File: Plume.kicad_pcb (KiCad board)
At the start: 4 copper layers, 0 parts

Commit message: Added RGB LED, added motor connectors, added test points, imported all 3D models
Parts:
- added C1001: 10u X5R 16V, Capacitor_SMD:C_0603_1608Metric, F.Cu at (188.8, 130.8)
- added C1002: 100n X7R 16V, Capacitor_SMD:C_0402_1005Metric, F.Cu at (192.2, 130.5)
- added C1003: 100n X7R 16V, Capacitor_SMD:C_0402_1005Metric, F.Cu at (192.2, 132.4)
- added C1101: 10u X5R 16V, Capacitor_SMD:C_0603_1608Metric, F.Cu at (188.7, 105.7)
- added C1102: 100n X7R 16V, Capacitor_SMD:C_0402_1005Metric, F.Cu at (185.2, 108.0)
- added C1103: 100n X7R 16V, Capacitor_SMD:C_0402_1005Metric, F.Cu at (185.2, 106.1)
- added C1201: 10u X5R 16V, Capacitor_SMD:C_0603_1608Metric, F.Cu at (200.4, 105.7)
- added C1202: 100n X7R 16V, Capacitor_SMD:C_0402_1005Metric, F.Cu at (196.9, 108.0)
- added C1203: 100n X7R 16V, Capacitor_SMD:C_0402_1005Metric, F.Cu at (196.9, 106.1)
- added C1301: 10u X5R 16V, Capacitor_SMD:C_0603_1608Metric, F.Cu at (188.7, 93.3)
- added C1302: 100n X7R 16V, Capacitor_SMD:C_0402_1005Metric, F.Cu at (185.2, 95.7)
- added C1303: 100n X7R 16V, Capacitor_SMD:C_0402_1005Metric, F.Cu at (185.2, 93.7)
- added C1401: 10u X5R 16V, Capacitor_SMD:C_0603_1608Metric, F.Cu at (200.4, 93.3)
- added C1402: 100n X7R 16V, Capacitor_SMD:C_0402_1005Metric, F.Cu at (196.9, 95.7)
- added C1403: 100n X7R 16V, Capacitor_SMD:C_0402_1005Metric, F.Cu at (196.9, 93.7)
- added C1501: 10u X5R 16V, Capacitor_SMD:C_0603_1608Metric, F.Cu at (165.1, 93.3)
- added C1502: 100n X7R 16V, Capacitor_SMD:C_0402_1005Metric, F.Cu at (161.6, 95.7)
- added C1503: 100n X7R 16V, Capacitor_SMD:C_0402_1005Metric, F.Cu at (161.6, 93.7)
- added C1601: 10u X5R 16V, Capacitor_SMD:C_0603_1608Metric, F.Cu at (176.9, 93.3)
- added C1602: 100n X7R 16V, Capacitor_SMD:C_0402_1005Metric, F.Cu at (173.4, 95.7)
- added C1603: 100n X7R 16V, Capacitor_SMD:C_0402_1005Metric, F.Cu at (173.4, 93.7)
- added C1701: 10u X5R 16V, Capacitor_SMD:C_0603_1608Metric, F.Cu at (176.9, 105.7)
- added C1702: 100n X7R 16V, Capacitor_SMD:C_0402_1005Metric, F.Cu at (173.4, 108.0)
- added C1703: 100n X7R 16V, Capacitor_SMD:C_0402_1005Metric, F.Cu at (173.4, 106.1)
- added C1801: 10u X5R 16V, Capacitor_SMD:C_0603_1608Metric, F.Cu at (188.7, 118.0)
- added C1802: 100n X7R 16V, Capacitor_SMD:C_0402_1005Metric, F.Cu at (185.2, 120.3)
- added C1803: 100n X7R 16V, Capacitor_SMD:C_0402_1005Metric, F.Cu at (185.2, 118.4)
- added C1901: 10u X5R 16V, Capacitor_SMD:C_0603_1608Metric, F.Cu at (153.3, 130.3)
- added C1902: 100n X7R 16V, Capacitor_SMD:C_0402_1005Metric, F.Cu at (149.9, 132.7)
- added C1903: 100n X7R 16V, Capacitor_SMD:C_0402_1005Metric, F.Cu at (149.9, 130.7)
- added C2001: 10u X5R 16V, Capacitor_SMD:C_0603_1608Metric, F.Cu at (153.3, 118.0)
- added C2002: 100n X7R 16V, Capacitor_SMD:C_0402_1005Metric, F.Cu at (149.9, 120.3)
- added C2003: 100n X7R 16V, Capacitor_SMD:C_0402_1005Metric, F.Cu at (149.9, 118.4)
- added C2101: 10u X5R 16V, Capacitor_SMD:C_0603_1608Metric, F.Cu at (153.3, 93.3)
- added C2102: 100n X7R 16V, Capacitor_SMD:C_0402_1005Metric, F.Cu at (149.9, 95.7)
- added C2103: 100n X7R 16V, Capacitor_SMD:C_0402_1005Metric, F.Cu at (149.9, 93.7)
- added C2201: 10u X5R 16V, Capacitor_SMD:C_0603_1608Metric, F.Cu at (165.1, 130.3)
- added C2202: 100n X7R 16V, Capacitor_SMD:C_0402_1005Metric, F.Cu at (161.6, 132.7)
- added C2203: 100n X7R 16V, Capacitor_SMD:C_0402_1005Metric, F.Cu at (161.6, 130.7)
- added C2301: 10u X5R 16V, Capacitor_SMD:C_0603_1608Metric, F.Cu at (153.3, 105.7)
- added C2302: 100n X7R 16V, Capacitor_SMD:C_0402_1005Metric, F.Cu at (149.9, 108.0)
- added C2303: 100n X7R 16V, Capacitor_SMD:C_0402_1005Metric, F.Cu at (149.9, 106.1)
- added C2401: 10u X5R 16V, Capacitor_SMD:C_0603_1608Metric, F.Cu at (165.1, 105.7)
- added C2402: 100n X7R 16V, Capacitor_SMD:C_0402_1005Metric, F.Cu at (161.6, 108.0)
- added C2403: 100n X7R 16V, Capacitor_SMD:C_0402_1005Metric, F.Cu at (161.6, 106.1)
- added C2501: 10u X5R 16V, Capacitor_SMD:C_0603_1608Metric, F.Cu at (176.9, 118.0)
- added C2502: 100n X7R 16V, Capacitor_SMD:C_0402_1005Metric, F.Cu at (173.4, 120.3)
- added C2503: 100n X7R 16V, Capacitor_SMD:C_0402_1005Metric, F.Cu at (173.4, 118.4)
- added C2601: 10u X5R 16V, Capacitor_SMD:C_0603_1608Metric, F.Cu at (165.1, 118.0)
- added C2602: 100n X7R 16V, Capacitor_SMD:C_0402_1005Metric, F.Cu at (161.6, 120.3)
- added C2603: 100n X7R 16V, Capacitor_SMD:C_0402_1005Metric, F.Cu at (161.6, 118.4)
- added C2701: 10u X5R 16V, Capacitor_SMD:C_0603_1608Metric, F.Cu at (176.9, 130.3)
- added C2702: 100n X7R 16V, Capacitor_SMD:C_0402_1005Metric, F.Cu at (173.4, 132.7)
- added C2703: 100n X7R 16V, Capacitor_SMD:C_0402_1005Metric, F.Cu at (173.4, 130.7)
- added C2801: 220n X7R 16V, Capacitor_SMD:C_0603_1608Metric, F.Cu at (192.3, 74.9)
- added C2802: 2u2 X7R 16V, Capacitor_SMD:C_0603_1608Metric, F.Cu at (192.3, 72.4)
- added C2803: 100n X7R 16V, Capacitor_SMD:C_0402_1005Metric, F.Cu at (199.7, 75.1)
- added C2804: 2u2 X7R 16V, Capacitor_SMD:C_0603_1608Metric, F.Cu at (192.3, 69.9)
- added C2901: 1n X7R 1kV, Capacitor_SMD:C_0603_1608Metric, F.Cu at (161.9, 47.3)
- added C2902: 1n X7R 1kV, Capacitor_SMD:C_0603_1608Metric, F.Cu at (161.9, 49.9)
- added C2903: 1n X7R 1kV, Capacitor_SMD:C_0603_1608Metric, F.Cu at (161.9, 52.4)
- added C2904: 1n X7R 1kV, Capacitor_SMD:C_0603_1608Metric, F.Cu at (161.9, 54.9)
- added C401: 100n X7R 16V, Capacitor_SMD:C_0402_1005Metric, F.Cu at (197.8, 52.1)
- added C402: 100n X7R 16V, Capacitor_SMD:C_0402_1005Metric, F.Cu at (197.8, 54.1)
- added C403: 4u7 X7R 16V, Capacitor_SMD:C_0603_1608Metric, F.Cu at (201.2, 52.4)
- added C404: 100n X7R 16V, Capacitor_SMD:C_0402_1005Metric, F.Cu at (197.8, 56.1)
- added C501: 4u7 X7R 16V, Capacitor_SMD:C_0603_1608Metric, F.Cu at (216.6, 60.7)
- added C502: 100n X7R 16V, Capacitor_SMD:C_0402_1005Metric, F.Cu at (220.6, 53.8)
- added C503: 4u7 X7R 16V, Capacitor_SMD:C_0603_1608Metric, F.Cu at (216.6, 58.2)
- added C601: 100n X7R 16V, Capacitor_SMD:C_0402_1005Metric, F.Cu at (171.4, 47.1)
- added C602: 10u X5R 16V, Capacitor_SMD:C_0603_1608Metric, F.Cu at (167.9, 59.9)
- added C603: 1u X7R 16V, Capacitor_SMD:C_0603_1608Metric, F.Cu at (167.9, 57.4)
- added C604: 100n X7R 16V, Capacitor_SMD:C_0402_1005Metric, F.Cu at (171.4, 49.0)
- added C605: 100n X7R 16V, Capacitor_SMD:C_0402_1005Metric, F.Cu at (171.4, 51.0)
- added C606: 470n X7R 25V, Capacitor_SMD:C_0603_1608Metric, F.Cu at (167.9, 47.3)
- added C607: 22n X7R 25V, Capacitor_SMD:C_0402_1005Metric, F.Cu at (171.4, 55.0)
- added C608: 10n C0G 25V, Capacitor_SMD:C_0402_1005Metric, F.Cu at (171.4, 58.9)
- added C609: 470n X7R 25V, Capacitor_SMD:C_0603_1608Metric, F.Cu at (167.9, 54.9)
- added C610: 470n X7R 25V, Capacitor_SMD:C_0603_1608Metric, F.Cu at (167.9, 52.4)
- added C611: 470n X7R 25V, Capacitor_SMD:C_0603_1608Metric, F.Cu at (167.9, 49.9)
- added C612: 22n X7R 25V, Capacitor_SMD:C_0402_1005Metric, F.Cu at (171.4, 53.0)
- added C613: 10n C0G 25V, Capacitor_SMD:C_0402_1005Metric, F.Cu at (171.4, 56.9)
- added C701: 100n X7R 16V, Capacitor_SMD:C_0402_1005Metric, F.Cu at (167.4, 80.0)
- added C702: 1u X7R 16V, Capacitor_SMD:C_0603_1608Metric, F.Cu at (171.0, 77.7)
- added C703: 10u X5R 16V, Capacitor_SMD:C_0603_1608Metric, F.Cu at (171.0, 80.3)
- added C801: 1u X7R 16V, Capacitor_SMD:C_0603_1608Metric, F.Cu at (213.5, 73.4)
- added C802: 100n X7R 16V, Capacitor_SMD:C_0402_1005Metric, F.Cu at (213.0, 75.6)
- added D2801: IN-PI22TAT5R5G5B, 0_Plume:INPI22TAT5R5G5B, F.Cu at (197.4, 71.4)
- added D601: TVS SMF5.0A, 0_Plume:D_SOD-123FL, F.Cu at (181.1, 63.2)
- added D701: Schottky 1N5819W, Diode_SMD:Nexperia_CFP3_SOD-123W, F.Cu at (168.7, 70.2)
- added H2901: M2.5 (2.7mm), MountingHole:MountingHole_2.5mm_Pad_Via, F.Cu at (156.6, 69.0)
- added H2902: M2.5 (2.7mm), MountingHole:MountingHole_2.5mm_Pad_Via, F.Cu at (156.6, 49.4)
- added H2903: M2.5 (2.7mm), MountingHole:MountingHole_2.5mm_Pad_Via, F.Cu at (156.6, 55.9)
- added H2904: M2.5 (2.7mm), MountingHole:MountingHole_2.5mm_Pad_Via, F.Cu at (156.6, 62.5)
- added IC1001: DRV8214RTER, 0_Plume:WQFN-16-1EP_3x3mm_P0.5mm_EP1.68x1.68mm_ThermalVias, F.Cu at (189.4, 126.8)
- added IC1101: DRV8214RTER, 0_Plume:WQFN-16-1EP_3x3mm_P0.5mm_EP1.68x1.68mm_ThermalVias, F.Cu at (189.3, 101.8)
- added IC1201: DRV8214RTER, 0_Plume:WQFN-16-1EP_3x3mm_P0.5mm_EP1.68x1.68mm_ThermalVias, F.Cu at (201.1, 101.8)
- added IC1301: DRV8214RTER, 0_Plume:WQFN-16-1EP_3x3mm_P0.5mm_EP1.68x1.68mm_ThermalVias, F.Cu at (189.3, 89.4)
- added IC1401: DRV8214RTER, 0_Plume:WQFN-16-1EP_3x3mm_P0.5mm_EP1.68x1.68mm_ThermalVias, F.Cu at (201.1, 89.4)
- added IC1501: DRV8214RTER, 0_Plume:WQFN-16-1EP_3x3mm_P0.5mm_EP1.68x1.68mm_ThermalVias, F.Cu at (165.8, 89.4)
- added IC1601: DRV8214RTER, 0_Plume:WQFN-16-1EP_3x3mm_P0.5mm_EP1.68x1.68mm_ThermalVias, F.Cu at (177.5, 89.4)
- added IC1701: DRV8214RTER, 0_Plume:WQFN-16-1EP_3x3mm_P0.5mm_EP1.68x1.68mm_ThermalVias, F.Cu at (177.5, 101.8)
- added IC1801: DRV8214RTER, 0_Plume:WQFN-16-1EP_3x3mm_P0.5mm_EP1.68x1.68mm_ThermalVias, F.Cu at (189.3, 114.1)
- added IC1901: DRV8214RTER, 0_Plume:WQFN-16-1EP_3x3mm_P0.5mm_EP1.68x1.68mm_ThermalVias, F.Cu at (154.0, 126.4)
- added IC2001: DRV8214RTER, 0_Plume:WQFN-16-1EP_3x3mm_P0.5mm_EP1.68x1.68mm_ThermalVias, F.Cu at (154.0, 114.1)
- added IC2101: DRV8214RTER, 0_Plume:WQFN-16-1EP_3x3mm_P0.5mm_EP1.68x1.68mm_ThermalVias, F.Cu at (154.0, 89.4)
- added IC2201: DRV8214RTER, 0_Plume:WQFN-16-1EP_3x3mm_P0.5mm_EP1.68x1.68mm_ThermalVias, F.Cu at (165.8, 126.4)
- added IC2301: DRV8214RTER, 0_Plume:WQFN-16-1EP_3x3mm_P0.5mm_EP1.68x1.68mm_ThermalVias, F.Cu at (154.0, 101.8)
- added IC2401: DRV8214RTER, 0_Plume:WQFN-16-1EP_3x3mm_P0.5mm_EP1.68x1.68mm_ThermalVias, F.Cu at (165.8, 101.8)
- added IC2501: DRV8214RTER, 0_Plume:WQFN-16-1EP_3x3mm_P0.5mm_EP1.68x1.68mm_ThermalVias, F.Cu at (177.5, 114.1)
- added IC2601: DRV8214RTER, 0_Plume:WQFN-16-1EP_3x3mm_P0.5mm_EP1.68x1.68mm_ThermalVias, F.Cu at (165.8, 114.1)
- added IC2701: DRV8214RTER, 0_Plume:WQFN-16-1EP_3x3mm_P0.5mm_EP1.68x1.68mm_ThermalVias, F.Cu at (177.5, 126.4)
- added IC2801: SN74AHCT1G125DRLR, 0_Plume:SOT-553, F.Cu at (192.5, 77.6)
- added IC2802: REG71050DRVT, 0_Plume:WSON-6-1EP_2x2mm_P0.65mm_EP1x1.6mm, F.Cu at (196.4, 76.0)
- added J401: Conn_ARM_SWD_TagConnect_TC2030-NL, Connector:Tag-Connect_TC2030-IDC-NL_2x03_P1.27mm_Vertical, F.Cu at (200.4, 48.6)
- added J501: S2B-PH-SM4-TB, 0_Plume:CONN_S2B-PH-SM4-TB_JST, F.Cu at (214.3, 51.6)
- added J601: USB_C_Receptacle_PowerOnly_6P, 0_Plume:USB4125-GF-A, F.Cu at (178.7, 51.1)
- added LED1001: BLUE, 0_Plume:KingBright_LED_0603, F.Cu at (240.1, 61.6)
- added LED1101: BLUE, 0_Plume:KingBright_LED_0603, F.Cu at (188.7, 108.2)
- added LED1201: BLUE, 0_Plume:KingBright_LED_0603, F.Cu at (200.4, 108.2)
- added LED1301: BLUE, 0_Plume:KingBright_LED_0603, F.Cu at (188.7, 95.9)
- added LED1401: BLUE, 0_Plume:KingBright_LED_0603, F.Cu at (200.4, 95.9)
- added LED1501: BLUE, 0_Plume:KingBright_LED_0603, F.Cu at (165.1, 95.9)
- added LED1601: BLUE, 0_Plume:KingBright_LED_0603, F.Cu at (176.9, 95.9)
- added LED1701: BLUE, 0_Plume:KingBright_LED_0603, F.Cu at (176.9, 108.2)
- added LED1801: BLUE, 0_Plume:KingBright_LED_0603, F.Cu at (188.7, 120.5)
- added LED1901: BLUE, 0_Plume:KingBright_LED_0603, F.Cu at (153.3, 132.8)
- added LED2001: BLUE, 0_Plume:KingBright_LED_0603, F.Cu at (153.3, 120.5)
- added LED2101: BLUE, 0_Plume:KingBright_LED_0603, F.Cu at (153.3, 95.9)
- added LED2201: BLUE, 0_Plume:KingBright_LED_0603, F.Cu at (165.1, 132.8)
- added LED2301: BLUE, 0_Plume:KingBright_LED_0603, F.Cu at (153.3, 108.2)
- added LED2401: BLUE, 0_Plume:KingBright_LED_0603, F.Cu at (165.1, 108.2)
- added LED2501: BLUE, 0_Plume:KingBright_LED_0603, F.Cu at (176.9, 120.5)
- added LED2601: BLUE, 0_Plume:KingBright_LED_0603, F.Cu at (165.1, 120.5)
- added LED2701: BLUE, 0_Plume:KingBright_LED_0603, F.Cu at (176.9, 132.8)
- added LED501: GREEN, 0_Plume:KingBright_LED_0603, F.Cu at (220.6, 58.2)
- added LED601: RED, 0_Plume:Bivar_LED_0603, F.Cu at (167.9, 62.4)
- added Q501: CSD85302L, 0_Plume:CSD85302L, F.Cu at (220.9, 51.1)
- added Q601: CSD75207W15, 0_Plume:Texas_DSBGA-9_1.62x1.58mm_Layout3x3_P0.5mm, F.Cu at (175.1, 64.3)
- added Q701: PMOS SI2365EDS-T1-GE3, Package_TO_SOT_SMD:SOT-23-3, F.Cu at (171.6, 74.3)
- added R1001: 680R 1%, Resistor_SMD:R_0402_1005Metric, F.Cu at (185.3, 125.2)
- added R1002: 330R 1%, Resistor_SMD:R_0402_1005Metric, F.Cu at (185.3, 127.2)
- added R1003: 100k 1%, Resistor_SMD:R_0402_1005Metric, F.Cu at (185.3, 129.2)
- added R1101: 680R 1%, Resistor_SMD:R_0402_1005Metric, F.Cu at (185.2, 100.1)
- added R1102: 330R 1%, Resistor_SMD:R_0402_1005Metric, F.Cu at (185.2, 104.1)
- added R1103: 100k 1%, Resistor_SMD:R_0402_1005Metric, F.Cu at (185.2, 102.1)
- added R1201: 680R 1%, Resistor_SMD:R_0402_1005Metric, F.Cu at (197.0, 100.1)
- added R1202: 330R 1%, Resistor_SMD:R_0402_1005Metric, F.Cu at (197.0, 104.1)
- added R1203: 100k 1%, Resistor_SMD:R_0402_1005Metric, F.Cu at (197.0, 102.1)
- added R1301: 680R 1%, Resistor_SMD:R_0402_1005Metric, F.Cu at (185.2, 87.8)
- added R1302: 330R 1%, Resistor_SMD:R_0402_1005Metric, F.Cu at (185.2, 91.8)
- added R1303: 100k 1%, Resistor_SMD:R_0402_1005Metric, F.Cu at (185.2, 89.8)
- added R1401: 680R 1%, Resistor_SMD:R_0402_1005Metric, F.Cu at (197.0, 87.8)
- added R1402: 330R 1%, Resistor_SMD:R_0402_1005Metric, F.Cu at (197.0, 91.8)
- added R1403: 100k 1%, Resistor_SMD:R_0402_1005Metric, F.Cu at (197.0, 89.8)
- added R1501: 680R 1%, Resistor_SMD:R_0402_1005Metric, F.Cu at (161.7, 87.8)
- added R1502: 330R 1%, Resistor_SMD:R_0402_1005Metric, F.Cu at (161.7, 91.8)
- added R1503: 100k 1%, Resistor_SMD:R_0402_1005Metric, F.Cu at (161.7, 89.8)
- added R1601: 680R 1%, Resistor_SMD:R_0402_1005Metric, F.Cu at (173.4, 87.8)
- added R1602: 330R 1%, Resistor_SMD:R_0402_1005Metric, F.Cu at (173.4, 91.8)
- added R1603: 100k 1%, Resistor_SMD:R_0402_1005Metric, F.Cu at (173.4, 89.8)
- added R1701: 680R 1%, Resistor_SMD:R_0402_1005Metric, F.Cu at (173.4, 100.1)
- added R1702: 330R 1%, Resistor_SMD:R_0402_1005Metric, F.Cu at (173.4, 104.1)
- added R1703: 100k 1%, Resistor_SMD:R_0402_1005Metric, F.Cu at (173.4, 102.1)
- added R1801: 680R 1%, Resistor_SMD:R_0402_1005Metric, F.Cu at (185.2, 112.4)
- added R1802: 330R 1%, Resistor_SMD:R_0402_1005Metric, F.Cu at (185.2, 116.4)
- added R1803: 100k 1%, Resistor_SMD:R_0402_1005Metric, F.Cu at (185.2, 114.4)
- added R1901: 680R 1%, Resistor_SMD:R_0402_1005Metric, F.Cu at (149.9, 124.7)
- added R1902: 330R 1%, Resistor_SMD:R_0402_1005Metric, F.Cu at (149.9, 128.7)
- added R1903: 100k 1%, Resistor_SMD:R_0402_1005Metric, F.Cu at (149.9, 126.7)
- added R2001: 680R 1%, Resistor_SMD:R_0402_1005Metric, F.Cu at (149.9, 112.4)
- added R2002: 330R 1%, Resistor_SMD:R_0402_1005Metric, F.Cu at (149.9, 116.4)
- added R2003: 100k 1%, Resistor_SMD:R_0402_1005Metric, F.Cu at (149.9, 114.4)
- added R2101: 680R 1%, Resistor_SMD:R_0402_1005Metric, F.Cu at (149.9, 87.8)
- added R2102: 330R 1%, Resistor_SMD:R_0402_1005Metric, F.Cu at (149.9, 91.8)
- added R2103: 100k 1%, Resistor_SMD:R_0402_1005Metric, F.Cu at (149.9, 89.8)
- added R2201: 680R 1%, Resistor_SMD:R_0402_1005Metric, F.Cu at (161.7, 124.7)
- added R2202: 330R 1%, Resistor_SMD:R_0402_1005Metric, F.Cu at (161.7, 128.7)
- added R2203: 100k 1%, Resistor_SMD:R_0402_1005Metric, F.Cu at (161.7, 126.7)
- added R2301: 680R 1%, Resistor_SMD:R_0402_1005Metric, F.Cu at (149.9, 100.1)
- added R2302: 330R 1%, Resistor_SMD:R_0402_1005Metric, F.Cu at (149.9, 104.1)
- added R2303: 100k 1%, Resistor_SMD:R_0402_1005Metric, F.Cu at (149.9, 102.1)
- added R2401: 680R 1%, Resistor_SMD:R_0402_1005Metric, F.Cu at (161.7, 100.1)
- added R2402: 330R 1%, Resistor_SMD:R_0402_1005Metric, F.Cu at (161.7, 104.1)
- added R2403: 100k 1%, Resistor_SMD:R_0402_1005Metric, F.Cu at (161.7, 102.1)
- added R2501: 680R 1%, Resistor_SMD:R_0402_1005Metric, F.Cu at (173.4, 112.4)
- added R2502: 330R 1%, Resistor_SMD:R_0402_1005Metric, F.Cu at (173.4, 116.4)
- added R2503: 100k 1%, Resistor_SMD:R_0402_1005Metric, F.Cu at (173.4, 114.4)
- added R2601: 680R 1%, Resistor_SMD:R_0402_1005Metric, F.Cu at (161.7, 112.4)
- added R2602: 330R 1%, Resistor_SMD:R_0402_1005Metric, F.Cu at (161.7, 116.4)
- added R2603: 100k 1%, Resistor_SMD:R_0402_1005Metric, F.Cu at (161.7, 114.4)
- added R2701: 680R 1%, Resistor_SMD:R_0402_1005Metric, F.Cu at (173.4, 124.7)
- added R2702: 330R 1%, Resistor_SMD:R_0402_1005Metric, F.Cu at (173.4, 128.7)
- added R2703: 100k 1%, Resistor_SMD:R_0402_1005Metric, F.Cu at (173.4, 126.7)
- added R2901: 0R 1%, Resistor_SMD:R_0603_1608Metric, F.Cu at (161.9, 57.4)
- added R2902: 0R 1%, Resistor_SMD:R_0603_1608Metric, F.Cu at (161.9, 59.9)
- added R2903: 0R 1%, Resistor_SMD:R_0603_1608Metric, F.Cu at (161.9, 62.4)
- added R2904: 0R 1%, Resistor_SMD:R_0603_1608Metric, F.Cu at (161.9, 64.9)
- added R401: 330R 1%, Resistor_SMD:R_0402_1005Metric, F.Cu at (200.7, 54.6)
- added R402: 5k1 1%, Resistor_SMD:R_0402_1005Metric, F.Cu at (200.7, 56.6)
- added R501: 330R 1%, Resistor_SMD:R_0402_1005Metric, F.Cu at (207.9, 47.1)
- added R502: 2k2 1%, Resistor_SMD:R_0402_1005Metric, F.Cu at (207.9, 49.1)
- added R503: 330R 1%, Resistor_SMD:R_0402_1005Metric, F.Cu at (207.9, 51.1)
- added R504: 4M99 1%, Resistor_SMD:R_0402_1005Metric, F.Cu at (207.9, 53.1)
- added R505: 4M99 1%, Resistor_SMD:R_0402_1005Metric, F.Cu at (207.9, 55.0)
- added R506: 5k1 1%, Resistor_SMD:R_0402_1005Metric, F.Cu at (207.9, 57.0)
- added R601: 330R 1%, Resistor_SMD:R_0402_1005Metric, F.Cu at (179.7, 56.5)
- added R602: 5k1 1%, Resistor_SMD:R_0402_1005Metric, F.Cu at (179.7, 58.5)
- added R603: 5k1 1%, Resistor_SMD:R_0402_1005Metric, F.Cu at (179.7, 60.5)
- added R701: 100k 1%, Resistor_SMD:R_0402_1005Metric, F.Cu at (167.4, 78.1)
- added R801: 100k 1%, Resistor_SMD:R_0402_1005Metric, F.Cu at (207.2, 66.8)
- added R802: 3k 1%, Resistor_SMD:R_0402_1005Metric, F.Cu at (207.2, 68.8)
- added R803: 3k 1%, Resistor_SMD:R_0402_1005Metric, F.Cu at (207.2, 70.8)
- added R804: 3k 1%, Resistor_SMD:R_0402_1005Metric, F.Cu at (207.2, 72.8)
- added R805: 3k 1%, Resistor_SMD:R_0402_1005Metric, F.Cu at (207.2, 74.8)
- added R806: 3k 1%, Resistor_SMD:R_0402_1005Metric, F.Cu at (207.2, 76.7)
- added R807: 3k 1%, Resistor_SMD:R_0402_1005Metric, F.Cu at (210.1, 66.8)
- added R808: 3k 1%, Resistor_SMD:R_0402_1005Metric, F.Cu at (210.1, 68.8)
- added R809: 3k 1%, Resistor_SMD:R_0402_1005Metric, F.Cu at (210.1, 70.8)
- added R810: 3k 1%, Resistor_SMD:R_0402_1005Metric, F.Cu at (210.1, 72.8)
- added R811: 3k 1%, Resistor_SMD:R_0402_1005Metric, F.Cu at (210.1, 74.8)
- added S401: B3U-1100P-B, 0_Plume:B3U1100PB, F.Cu at (231.3, 62.7)
- added S402: B3U-1100P-B, 0_Plume:B3U1100PB, F.Cu at (231.3, 68.0)
- added TP1001: nFAULT, 0_Plume:TestPoint_Pad_D0.5mm_Back, F.Cu at (237.3, 61.1)
- added TP1002: RC_OUT, 0_Plume:TestPoint_Pad_D0.5mm_Back, F.Cu at (237.3, 62.7)
- added TP1003: OUT1, 0_Plume:TestPoint_Pad_D0.5mm_Back, F.Cu at (194.7, 117.3)
- added TP1004: OUT2, 0_Plume:TestPoint_Pad_D0.5mm_Back, F.Cu at (194.7, 118.9)
- added TP1101: nFAULT, 0_Plume:TestPoint_Pad_D0.5mm_Back, F.Cu at (183.0, 99.9)
- added TP1102: RC_OUT, 0_Plume:TestPoint_Pad_D0.5mm_Back, F.Cu at (183.0, 101.4)
- added TP1103: OUT1, 0_Plume:TestPoint_Pad_D0.5mm_Back, F.Cu at (183.0, 103.0)
- added TP1104: OUT2, 0_Plume:TestPoint_Pad_D0.5mm_Back, F.Cu at (183.0, 104.6)
- added TP1201: nFAULT, 0_Plume:TestPoint_Pad_D0.5mm_Back, F.Cu at (194.7, 99.9)
- added TP1202: RC_OUT, 0_Plume:TestPoint_Pad_D0.5mm_Back, F.Cu at (194.7, 101.4)
- added TP1203: OUT1, 0_Plume:TestPoint_Pad_D0.5mm_Back, F.Cu at (194.7, 103.0)
- added TP1204: OUT2, 0_Plume:TestPoint_Pad_D0.5mm_Back, F.Cu at (194.7, 104.6)
- added TP1301: nFAULT, 0_Plume:TestPoint_Pad_D0.5mm_Back, F.Cu at (183.0, 87.6)
- added TP1302: RC_OUT, 0_Plume:TestPoint_Pad_D0.5mm_Back, F.Cu at (183.0, 89.1)
- added TP1303: OUT1, 0_Plume:TestPoint_Pad_D0.5mm_Back, F.Cu at (183.0, 90.7)
- added TP1304: OUT2, 0_Plume:TestPoint_Pad_D0.5mm_Back, F.Cu at (183.0, 92.2)
- added TP1401: nFAULT, 0_Plume:TestPoint_Pad_D0.5mm_Back, F.Cu at (194.7, 87.6)
- added TP1402: RC_OUT, 0_Plume:TestPoint_Pad_D0.5mm_Back, F.Cu at (194.7, 89.1)
- added TP1403: OUT1, 0_Plume:TestPoint_Pad_D0.5mm_Back, F.Cu at (194.7, 90.7)
- added TP1404: OUT2, 0_Plume:TestPoint_Pad_D0.5mm_Back, F.Cu at (194.7, 92.2)
- added TP1501: nFAULT, 0_Plume:TestPoint_Pad_D0.5mm_Back, F.Cu at (159.4, 87.6)
- added TP1502: RC_OUT, 0_Plume:TestPoint_Pad_D0.5mm_Back, F.Cu at (159.4, 89.1)
- added TP1503: OUT1, 0_Plume:TestPoint_Pad_D0.5mm_Back, F.Cu at (159.4, 90.7)
- added TP1504: OUT2, 0_Plume:TestPoint_Pad_D0.5mm_Back, F.Cu at (159.4, 92.2)
- added TP1601: nFAULT, 0_Plume:TestPoint_Pad_D0.5mm_Back, F.Cu at (171.2, 87.6)
- added TP1602: RC_OUT, 0_Plume:TestPoint_Pad_D0.5mm_Back, F.Cu at (171.2, 89.1)
- added TP1603: OUT1, 0_Plume:TestPoint_Pad_D0.5mm_Back, F.Cu at (171.2, 90.7)
- added TP1604: OUT2, 0_Plume:TestPoint_Pad_D0.5mm_Back, F.Cu at (171.2, 92.2)
- added TP1701: nFAULT, 0_Plume:TestPoint_Pad_D0.5mm_Back, F.Cu at (171.2, 99.9)
- added TP1702: RC_OUT, 0_Plume:TestPoint_Pad_D0.5mm_Back, F.Cu at (171.2, 101.4)
- added TP1703: OUT1, 0_Plume:TestPoint_Pad_D0.5mm_Back, F.Cu at (171.2, 103.0)
- added TP1704: OUT2, 0_Plume:TestPoint_Pad_D0.5mm_Back, F.Cu at (171.2, 104.6)
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
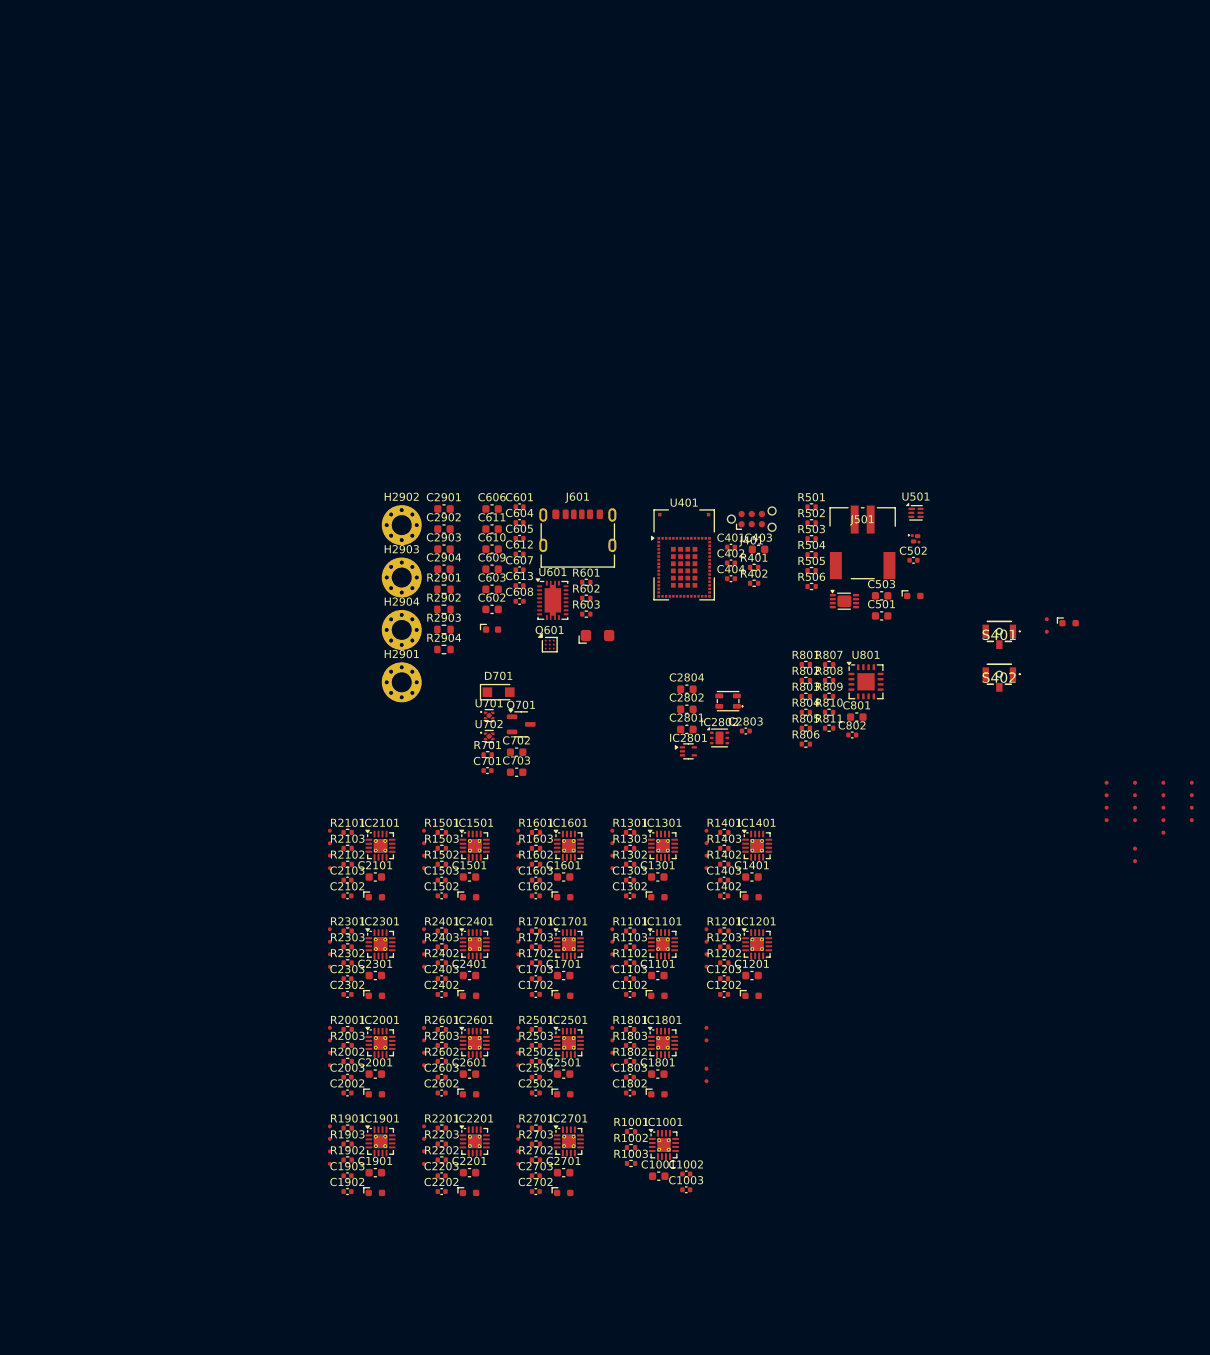
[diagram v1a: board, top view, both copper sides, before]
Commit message: Finished schematic, imported all footprints, all 3D models and created STM32 project, now need to proofread shematic before layout
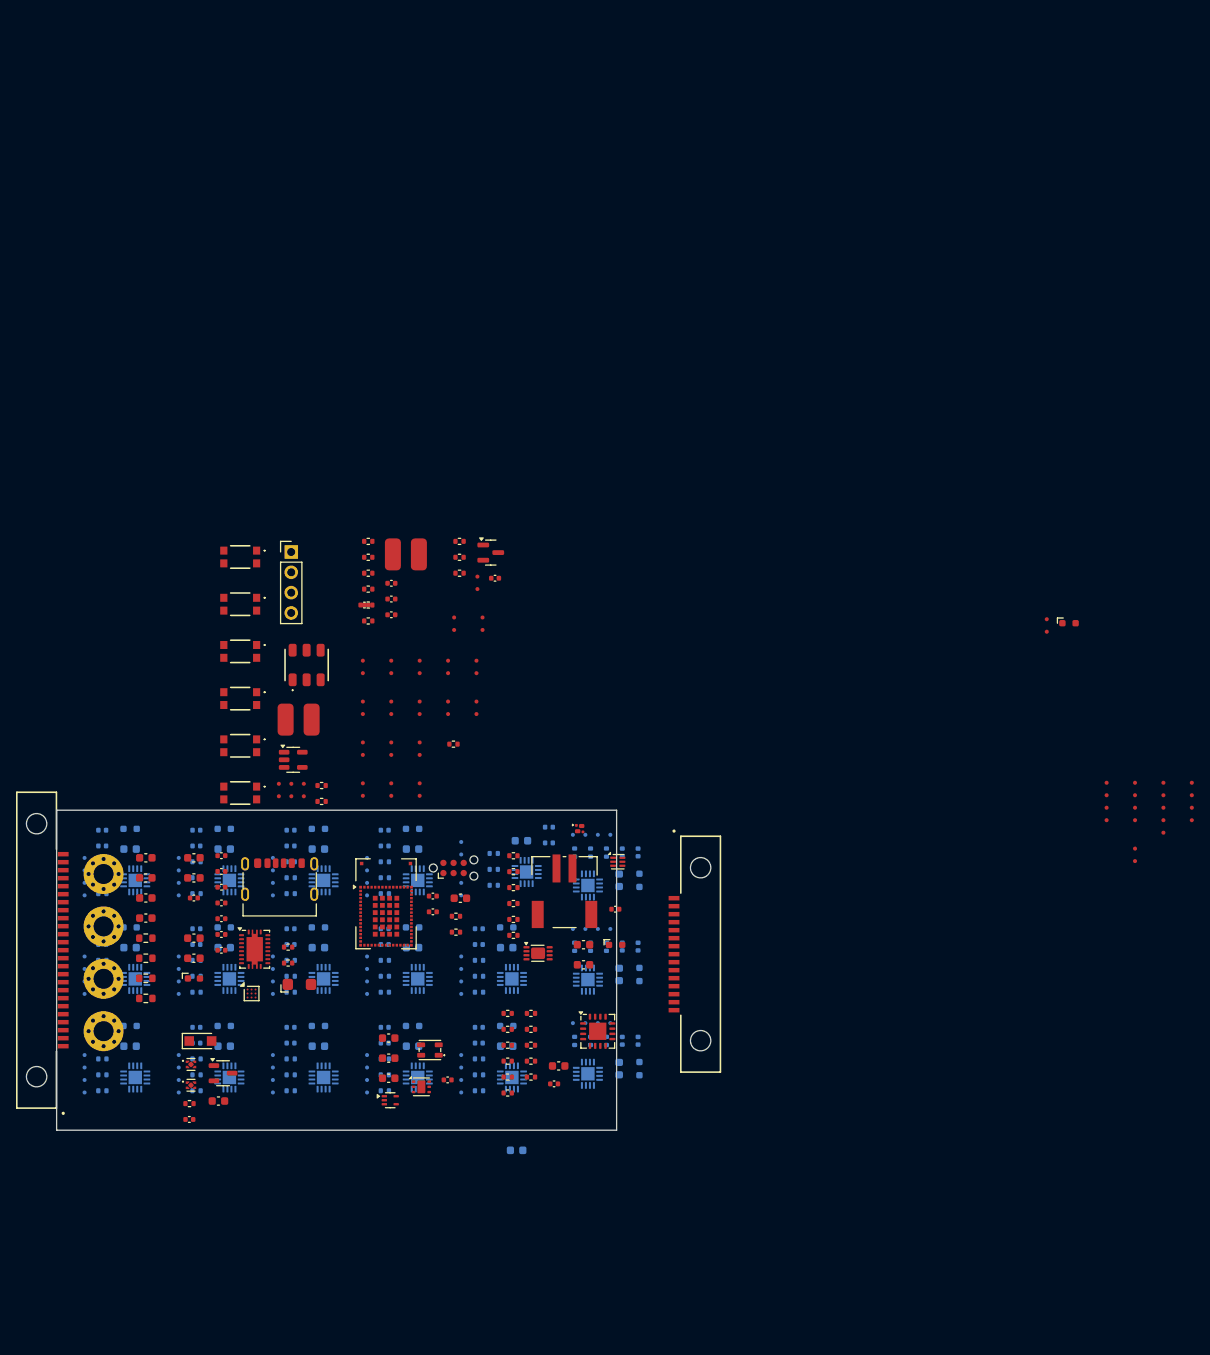
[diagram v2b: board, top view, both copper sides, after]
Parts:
- removed C404: 100n X7R 16V, Capacitor_SMD:C_0402_1005Metric
- removed the C609 at (167.9, 54.9)
- removed S401, S402: B3U-1100P-B, 0_Plume:B3U1100PB
- added C502: 100n X7R 16V, Capacitor_SMD:C_0402_1005Metric, F.Cu at (168.3, 56.0)
- added C606: 10n C0G 25V, Capacitor_SMD:C_0402_1005Metric, F.Cu at (155.3, 56.6)
- added C610: 150n X7R 25V, Capacitor_SMD:C_0402_1005Metric, F.Cu at (155.3, 58.6)
- added C612: 390pF X7R 25V, Capacitor_SMD:C_0402_1005Metric, F.Cu at (155.3, 60.6)
- added C616: 100n X7R 16V, Capacitor_SMD:C_0402_1005Metric, F.Cu at (152.0, 59.4)
- added D401: ESDS314, Package_TO_SOT_SMD:SOT-23-5, F.Cu at (143.1, 78.7)
- added J401: Solder Holes 4x1 2.54mm 22AWG, Connector_PinHeader_2.54mm:PinHeader_1x04_P2.54mm_Vertical, F.Cu at (142.8, 52.7)
- added J403: Solder Wire Pad 2x4mm, 0_Plume:SolderWirePad_SMD_2x4mm, F.Cu at (142.1, 73.7)
- added J404: Solder Wire Pad 2x4mm, 0_Plume:SolderWirePad_SMD_2x4mm, F.Cu at (145.4, 73.7)
- added J602: Solder Wire Pad 2x4mm, 0_Plume:SolderWirePad_SMD_2x4mm, F.Cu at (155.5, 53.0)
- added J603: Solder Wire Pad 2x4mm, 0_Plume:SolderWirePad_SMD_2x4mm, F.Cu at (158.8, 53.0)
- added J901: SEI-125-02-GF-S-M-AT, 0_Plume:SAMTEC_SEI-125-02-GF-S-M-AT, F.Cu at (111.0, 102.5)
- added J902: SEI-115-02-GF-S-M-AT, 0_Plume:SAMTEC_SEI-115-02-GF-S-M-AT, F.Cu at (194.0, 103.0)
- added Q501: NMOS IRLML6344TRPBF SOT-23, Package_TO_SOT_SMD:SOT-23, F.Cu at (167.8, 52.8)
- added R2801: 100k 1%, Resistor_SMD:R_0402_1005Metric, F.Cu at (163.1, 76.7)
- added R403: 22R 1%, Resistor_SMD:R_0402_1005Metric, F.Cu at (146.6, 81.9)
- added R404: 22R 1%, Resistor_SMD:R_0402_1005Metric, F.Cu at (146.6, 83.9)
- added R502: 3k 1%, Resistor_SMD:R_0402_1005Metric, F.Cu at (163.9, 51.4)
- added R503: 10k 1%, Resistor_SMD:R_0402_1005Metric, F.Cu at (163.9, 53.4)
- added R509: 100k 1%, Resistor_SMD:R_0402_1005Metric, F.Cu at (163.9, 55.4)
- added R604: 196R 1%, Resistor_SMD:R_0402_1005Metric, F.Cu at (152.5, 53.4)
- added R605: 10k 1%, Resistor_SMD:R_0402_1005Metric, F.Cu at (152.5, 55.4)
- added R606: 10k 1%, Resistor_SMD:R_0402_1005Metric, F.Cu at (152.5, 57.4)
- added R607: 196R 1%, Resistor_SMD:R_0402_1005Metric, F.Cu at (152.5, 59.4)
- added R608: 10k 1%, Resistor_SMD:R_0402_1005Metric, F.Cu at (152.5, 61.3)
- added SW401: KMR232NG ULC, 0_Plume:KMR232NGULCLFS, F.Cu at (136.4, 53.4)
- added SW402: KMR232NG ULC, 0_Plume:KMR232NGULCLFS, F.Cu at (136.4, 59.2)
- added SW403: CAS-D20A1, 0_Plume:CAS-D2xx, F.Cu at (144.8, 66.8)
- added SW404: KMR232NG ULC, 0_Plume:KMR232NGULCLFS, F.Cu at (136.4, 65.2)
- added SW405: KMR232NG ULC, 0_Plume:KMR232NGULCLFS, F.Cu at (136.4, 71.0)
- added SW406: KMR232NG ULC, 0_Plume:KMR232NGULCLFS, F.Cu at (136.4, 77.0)
- added SW407: KMR232NG ULC, 0_Plume:KMR232NGULCLFS, F.Cu at (136.4, 82.8)
- added TP1005: A0, 0_Plume:TestPoint_Pad_D0.5mm_Back, F.Cu at (151.8, 71.4)
- added TP1006: A1, 0_Plume:TestPoint_Pad_D0.5mm_Back, F.Cu at (151.8, 73.0)
- added TP1105: A0, 0_Plume:TestPoint_Pad_D0.5mm_Back, F.Cu at (158.9, 71.4)
- added TP1106: A1, 0_Plume:TestPoint_Pad_D0.5mm_Back, F.Cu at (158.9, 73.0)
- added TP1205: A0, 0_Plume:TestPoint_Pad_D0.5mm_Back, F.Cu at (162.4, 71.4)
- added TP1206: A1, 0_Plume:TestPoint_Pad_D0.5mm_Back, F.Cu at (162.4, 73.0)
- added TP1305: A0, 0_Plume:TestPoint_Pad_D0.5mm_Back, F.Cu at (158.9, 66.3)
- added TP1306: A1, 0_Plume:TestPoint_Pad_D0.5mm_Back, F.Cu at (158.9, 67.9)
- added TP1405: A0, 0_Plume:TestPoint_Pad_D0.5mm_Back, F.Cu at (162.4, 66.3)
- added TP1406: A1, 0_Plume:TestPoint_Pad_D0.5mm_Back, F.Cu at (162.4, 67.9)
- added TP1505: A0, 0_Plume:TestPoint_Pad_D0.5mm_Back, F.Cu at (151.8, 81.6)
- added TP1506: A1, 0_Plume:TestPoint_Pad_D0.5mm_Back, F.Cu at (151.8, 83.2)
- added TP1605: A0, 0_Plume:TestPoint_Pad_D0.5mm_Back, F.Cu at (155.3, 66.3)
- added TP1606: A1, 0_Plume:TestPoint_Pad_D0.5mm_Back, F.Cu at (155.3, 67.9)
- added TP1705: A0, 0_Plume:TestPoint_Pad_D0.5mm_Back, F.Cu at (155.3, 81.6)
- added TP1706: A1, 0_Plume:TestPoint_Pad_D0.5mm_Back, F.Cu at (155.3, 83.2)
- added TP1805: A0, 0_Plume:TestPoint_Pad_D0.5mm_Back, F.Cu at (158.9, 81.6)
- added TP1806: A1, 0_Plume:TestPoint_Pad_D0.5mm_Back, F.Cu at (158.9, 83.2)
- added TP1905: A0, 0_Plume:TestPoint_Pad_D0.5mm_Back, F.Cu at (151.8, 76.5)
- added TP1906: A1, 0_Plume:TestPoint_Pad_D0.5mm_Back, F.Cu at (151.8, 78.1)
- added TP2005: A0, 0_Plume:TestPoint_Pad_D0.5mm_Back, F.Cu at (151.8, 66.3)
- added TP2006: A1, 0_Plume:TestPoint_Pad_D0.5mm_Back, F.Cu at (151.8, 67.9)
- added TP2105: A0, 0_Plume:TestPoint_Pad_D0.5mm_Back, F.Cu at (163.2, 60.9)
- added TP2106: A1, 0_Plume:TestPoint_Pad_D0.5mm_Back, F.Cu at (163.2, 62.5)
- added TP2205: A0, 0_Plume:TestPoint_Pad_D0.5mm_Back, F.Cu at (155.3, 76.5)
- added TP2206: A1, 0_Plume:TestPoint_Pad_D0.5mm_Back, F.Cu at (155.3, 78.1)
- added TP2305: A0, 0_Plume:TestPoint_Pad_D0.5mm_Back, F.Cu at (166.7, 60.9)
- added TP2306: A1, 0_Plume:TestPoint_Pad_D0.5mm_Back, F.Cu at (166.7, 62.5)
- added TP2405: A0, 0_Plume:TestPoint_Pad_D0.5mm_Back, F.Cu at (166.0, 66.3)
- added TP2406: A1, 0_Plume:TestPoint_Pad_D0.5mm_Back, F.Cu at (166.0, 67.9)
- added TP2505: A0, 0_Plume:TestPoint_Pad_D0.5mm_Back, F.Cu at (166.0, 71.4)
- added TP2506: A1, 0_Plume:TestPoint_Pad_D0.5mm_Back, F.Cu at (166.0, 73.0)
- added TP2605: A0, 0_Plume:TestPoint_Pad_D0.5mm_Back, F.Cu at (155.3, 71.4)
- added TP2606: A1, 0_Plume:TestPoint_Pad_D0.5mm_Back, F.Cu at (155.3, 73.0)
- added TP2705: A0, 0_Plume:TestPoint_Pad_D0.5mm_Back, F.Cu at (158.9, 76.5)
- added TP2706: A1, 0_Plume:TestPoint_Pad_D0.5mm_Back, F.Cu at (158.9, 78.1)
- added TP401: BUTTON1, 0_Plume:TestPoint_Pad_D0.5mm_Back, F.Cu at (141.3, 81.7)
- added TP402: BUTTON2, 0_Plume:TestPoint_Pad_D0.5mm_Back, F.Cu at (141.3, 83.3)
- added TP403: BUTTON3, 0_Plume:TestPoint_Pad_D0.5mm_Back, F.Cu at (142.8, 81.7)
- added TP404: BUTTON4, 0_Plume:TestPoint_Pad_D0.5mm_Back, F.Cu at (142.8, 83.3)
- added TP405: SWITCH1, 0_Plume:TestPoint_Pad_D0.5mm_Back, F.Cu at (144.4, 81.7)
- added TP406: SWITCH2, 0_Plume:TestPoint_Pad_D0.5mm_Back, F.Cu at (144.4, 83.3)
- added TP504: BAT_SENSE_EN, 0_Plume:TestPoint_Pad_D0.5mm_Back, F.Cu at (166.1, 55.8)
- added TP505: BAT_SENSE, 0_Plume:TestPoint_Pad_D0.5mm_Back, F.Cu at (166.1, 57.4)
- C1001, C1002, C1003, C1101, C1102, C1103, C1201, C1202, C1203, C1301, C1302, C1303, C1401, C1402, C1403, C1501, C1502, C1503, C1601, C1602, C1603, C1701, C1702, C1703, C1801, C1802, C1803, C1901, C1902, C1903, C2001, C2002, C2003, C2101, C2102, C2103, C2201, C2202, C2203, C2301, C2302, C2303, C2401, C2402, C2403, C2501, C2502, C2503, C2601, C2602, C2603, C2701, C2702, C2703, C703, IC1001, IC1101, IC1201, IC1301, IC1401, IC1501, IC1601, IC1701, IC1801, IC1901, IC2001, IC2101, IC2201, IC2301, IC2401, IC2501, IC2601, IC2701, LED1101, LED1201, LED1301, LED1401, LED1501, LED1601, LED1701, LED1801, LED1901, LED2001, LED2101, LED2201, LED2301, LED2401, LED2501, LED2601, LED2701, R1001, R1002, R1003, R1101, R1102, R1103, R1201, R1202, R1203, R1301, R1302, R1303, R1401, R1402, R1403, R1501, R1502, R1503, R1601, R1602, R1603, R1701, R1702, R1703, R1801, R1802, R1803, R1901, R1902, R1903, R2001, R2002, R2003, R2101, R2102, R2103, R2201, R2202, R2203, R2301, R2302, R2303, R2401, R2402, R2403, R2501, R2502, R2503, R2601, R2602, R2603, R2701, R2702, R2703, TP1003, TP1004, TP1101, TP1102, TP1103, TP1104, TP1201, TP1202, TP1203, TP1204, TP1301, TP1302, TP1303, TP1304, TP1401, TP1402, TP1403, TP1404, TP1501, TP1502, TP1503, TP1504, TP1601, TP1602, TP1603, TP1604, TP1701, TP1702, TP1703, TP1704, TP1801, TP1802, TP1803, TP1804, TP1901, TP1902, TP1903, TP1904, TP2001, TP2002, TP2003, TP2004, TP2101, TP2102, TP2103, TP2104, TP2201, TP2202, TP2203, TP2204, TP2301, TP2302, TP2303, TP2304, TP2401, TP2402, TP2403, TP2404, TP2501, TP2502, TP2503, TP2504, TP2601, TP2602, TP2603, TP2604, TP2701, TP2702, TP2703, TP2704, TP901, TP902: moved to B.Cu
- C611: renamed from C610; value 470n X7R 25V -> 2n2 X7R 25V; footprint Capacitor_SMD:C_0603_1608Metric -> Capacitor_SMD:C_0402_1005Metric
- R601: value 330R 1% -> 680R 1%
- U401: value STM32WB5MMG -> STM32WB5MMGH6TR
- moved U502 58.3 mm to (173.7, 102.9)
- moved C603 57.4 mm to (130.7, 101.0)
- moved C613 57.4 mm to (130.7, 93.5)
- moved D601 57.4 mm to (143.8, 106.8)
- moved R402 57.4 mm to (163.4, 100.2)
- moved R506 57.4 mm to (170.6, 96.7)
- moved R603 57.4 mm to (142.4, 104.1)
- moved C2801 57.4 mm to (155.0, 118.5)
- moved C2802 57.4 mm to (155.0, 116.0)
- moved C2803 57.4 mm to (162.4, 118.7)
- moved C2804 57.4 mm to (155.0, 113.5)
- moved C401 57.4 mm to (160.5, 95.7)
- moved C402 57.4 mm to (160.5, 97.7)
- moved C403 57.4 mm to (164.0, 96.0)
- moved C503 57.4 mm to (183.3, 97.4)
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- renumbered C502 to C503, C503 to C504, C606 to C607, C607 to C608, C608 to C609, C611 to C613, C612 to C614, C613 to C615, J401 to J402, Q501 to Q502, R502 to R504, R503 to R505, R504 to R506, R505 to R507, R506 to R508, TP504 to TP506, TP505 to TP507
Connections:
- net /Project Architecture/Logic - I2C Mux/SCL renamed /Project Architecture/Logic - I2C Mux/I2C1_SCL
- net /Project Architecture/Logic - I2C Mux/SDA renamed /Project Architecture/Logic - I2C Mux/I2C1_SDA
- net /Project Architecture/Motor Control - Drivers/nSLEEP_FRONT renamed /Project Architecture/MCU - Unit/nSLEEP_FRONT
- net /Project Architecture/Motor Control - Drivers/nSLEEP_REAR renamed /Project Architecture/MCU - Unit/nSLEEP_BACK
- net /Project Architecture/Power - Battery Management/CHARGE_STATUS renamed /Project Architecture/MCU - Unit/CHARGE_STATUS
- net /Project Architecture/User - RGB LED Indicator/5V_ENABLE renamed /Project Architecture/MCU - Unit/5V_ENABLE
- net /Project Architecture/User - RGB LED Indicator/DIN_3V3 renamed /Project Architecture/MCU - Unit/DIN_3V3
- net Net-(U401B-PH3-BOOT0) renamed /Project Architecture/MCU - Unit/BOOT0
- C402 pad 1: Net-(U401B-NRST) -> /Project Architecture/MCU - Unit/~{RESET}
- J402 pad 1: unconnected-(J401-VCC-Pad1) -> +3V3
- J402 pad 2: unconnected-(J401-SWDIO-Pad2) -> /Project Architecture/MCU - Unit/SWDIO
- J402 pad 3: unconnected-(J401-~{RESET}-Pad3) -> /Project Architecture/MCU - Unit/~{RESET}
- J402 pad 4: unconnected-(J401-SWCLK-Pad4) -> /Project Architecture/MCU - Unit/SWCLK
- J402 pad 5: unconnected-(J401-GND-Pad5) -> GND
- J402 pad 6: unconnected-(J401-SWO-Pad6) -> /Project Architecture/MCU - Unit/SWO
- U401 pad 10: Net-(U401B-NRST) -> /Project Architecture/MCU - Unit/~{RESET}
- U401 pad 11: unconnected-(U401A-PB9-Pad11) -> /Project Architecture/MCU - Unit/I2C1_SDA
- U401 pad 12: unconnected-(U401A-PC0-Pad12) -> /Project Architecture/MCU - Unit/I2C3_SCL
- U401 pad 14: unconnected-(U401A-PB8-Pad14) -> /Project Architecture/MCU - Unit/I2C1_SCL
- U401 pad 21: unconnected-(U401A-PB3-Pad21) -> /Project Architecture/MCU - Unit/SWO
- U401 pad 25: unconnected-(U401A-PA13-Pad25) -> /Project Architecture/MCU - Unit/SWDIO
- U401 pad 26: unconnected-(U401A-PA14-Pad26) -> /Project Architecture/MCU - Unit/SWCLK
- U401 pad 28: unconnected-(U401A-PA10-Pad28) -> Net-(U401A-PA10)
- U401 pad 33: unconnected-(U401A-PD0-Pad33) -> /Project Architecture/Motor Control - Drivers/Motor Control - Driver 17/nFAULT
- U401 pad 34: unconnected-(U401A-PD1-Pad34) -> /Project Architecture/Motor Control - Drivers/Motor Control - Driver 16/nFAULT
- U401 pad 35: unconnected-(U401A-PB13-Pad35) -> /Project Architecture/Motor Control - Drivers/Motor Control - Driver 15/nFAULT
- U401 pad 36: unconnected-(U401A-PC6-Pad36) -> /Project Architecture/Motor Control - Drivers/Motor Control - Driver 14/nFAULT
- U401 pad 37: unconnected-(U401A-PB14-Pad37) -> /Project Architecture/Motor Control - Drivers/Motor Control - Driver 13/nFAULT
- U401 pad 38: unconnected-(U401A-PB15-Pad38) -> /Project Architecture/Motor Control - Drivers/Motor Control - Driver 12/nFAULT
- U401 pad 39: unconnected-(U401A-PB6-Pad39) -> /Project Architecture/Motor Control - Drivers/Motor Control - Driver 10/nFAULT
- U401 pad 40: unconnected-(U401A-PC13-Pad40) -> /Project Architecture/Motor Control - Drivers/Motor Control - Driver 11/nFAULT
- U401 pad 41: unconnected-(U401A-PB12-Pad41) -> /Project Architecture/Motor Control - Drivers/Motor Control - Driver 9/nFAULT
- U401 pad 42: unconnected-(U401A-PE4-Pad42) -> /Project Architecture/Motor Control - Drivers/Motor Control - Driver 8/nFAULT
- U401 pad 43: unconnected-(U401A-PB1-Pad43) -> /Project Architecture/Motor Control - Drivers/Motor Control - Driver 7/nFAULT
- U401 pad 44: unconnected-(U401A-PB0-Pad44) -> /Project Architecture/Motor Control - Drivers/Motor Control - Driver 6/nFAULT
- U401 pad 45: unconnected-(U401A-PC5-Pad45) -> /Project Architecture/Motor Control - Drivers/Motor Control - Driver 5/nFAULT
- U401 pad 46: unconnected-(U401A-PB11-Pad46) -> /Project Architecture/Motor Control - Drivers/Motor Control - Driver 4/nFAULT
- U401 pad 47: unconnected-(U401A-PB10-Pad47) -> /Project Architecture/Motor Control - Drivers/Motor Control - Driver 3/nFAULT
- U401 pad 48: unconnected-(U401A-PB2-Pad48) -> /Project Architecture/Motor Control - Drivers/Motor Control - Driver 2/nFAULT
- U401 pad 49: unconnected-(U401A-PC4-Pad49) -> /Project Architecture/Motor Control - Drivers/Motor Control - Driver 1/nFAULT
- U401 pad 50: unconnected-(U401A-PA8-Pad50) -> /Project Architecture/Motor Control - Drivers/Motor Control - Driver 0/nFAULT
- U401 pad 51: unconnected-(U401A-PA9-Pad51) -> Net-(U401A-PA9)
- U401 pad 62: (no net) -> unconnected-(U401A-PH1-Pad62)
- U401 pad 9: unconnected-(U401A-PC1-Pad9) -> /Project Architecture/MCU - Unit/I2C3_SDA
- U502 pad 1: unconnected-(U502-V_{DD}-Pad1) -> /Project Architecture/Power - Wireless Receiver & USB/+VCHARGE
- U502 pad 9: (no net) -> GND
- U801 pad 17: (no net) -> GND
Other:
- board outline added: 70 x 40 mm
- copper layers 4 -> 6
